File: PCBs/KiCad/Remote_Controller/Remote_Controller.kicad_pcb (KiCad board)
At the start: 2 copper layers, 83 parts, among them J201 USB_C_Receptacle_USB2.0_16P, Q101 IRF7309IPBF, Q102 IRFML8244TRPBF, Q103 IRFML8244TRPBF, Q201 SS8050-G, Q202 SS8050-G, SW101 Power Switch, SW201 SW_Push, SW301 SW_Push, SW302 SW_Push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

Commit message: Add board rules and stack up
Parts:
- Q101: value IRF7309IPBF -> IRF7319
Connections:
- net Net-(Q101A-G) renamed /[1] Power/PW_SW_R
- net Net-(Q101A-S) renamed /[1] Power/PW_SW_R_G_S
- net Net-(SW101-A) renamed /[1] Power/PWR_SW_CAP
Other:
- copper layers 2 -> 4

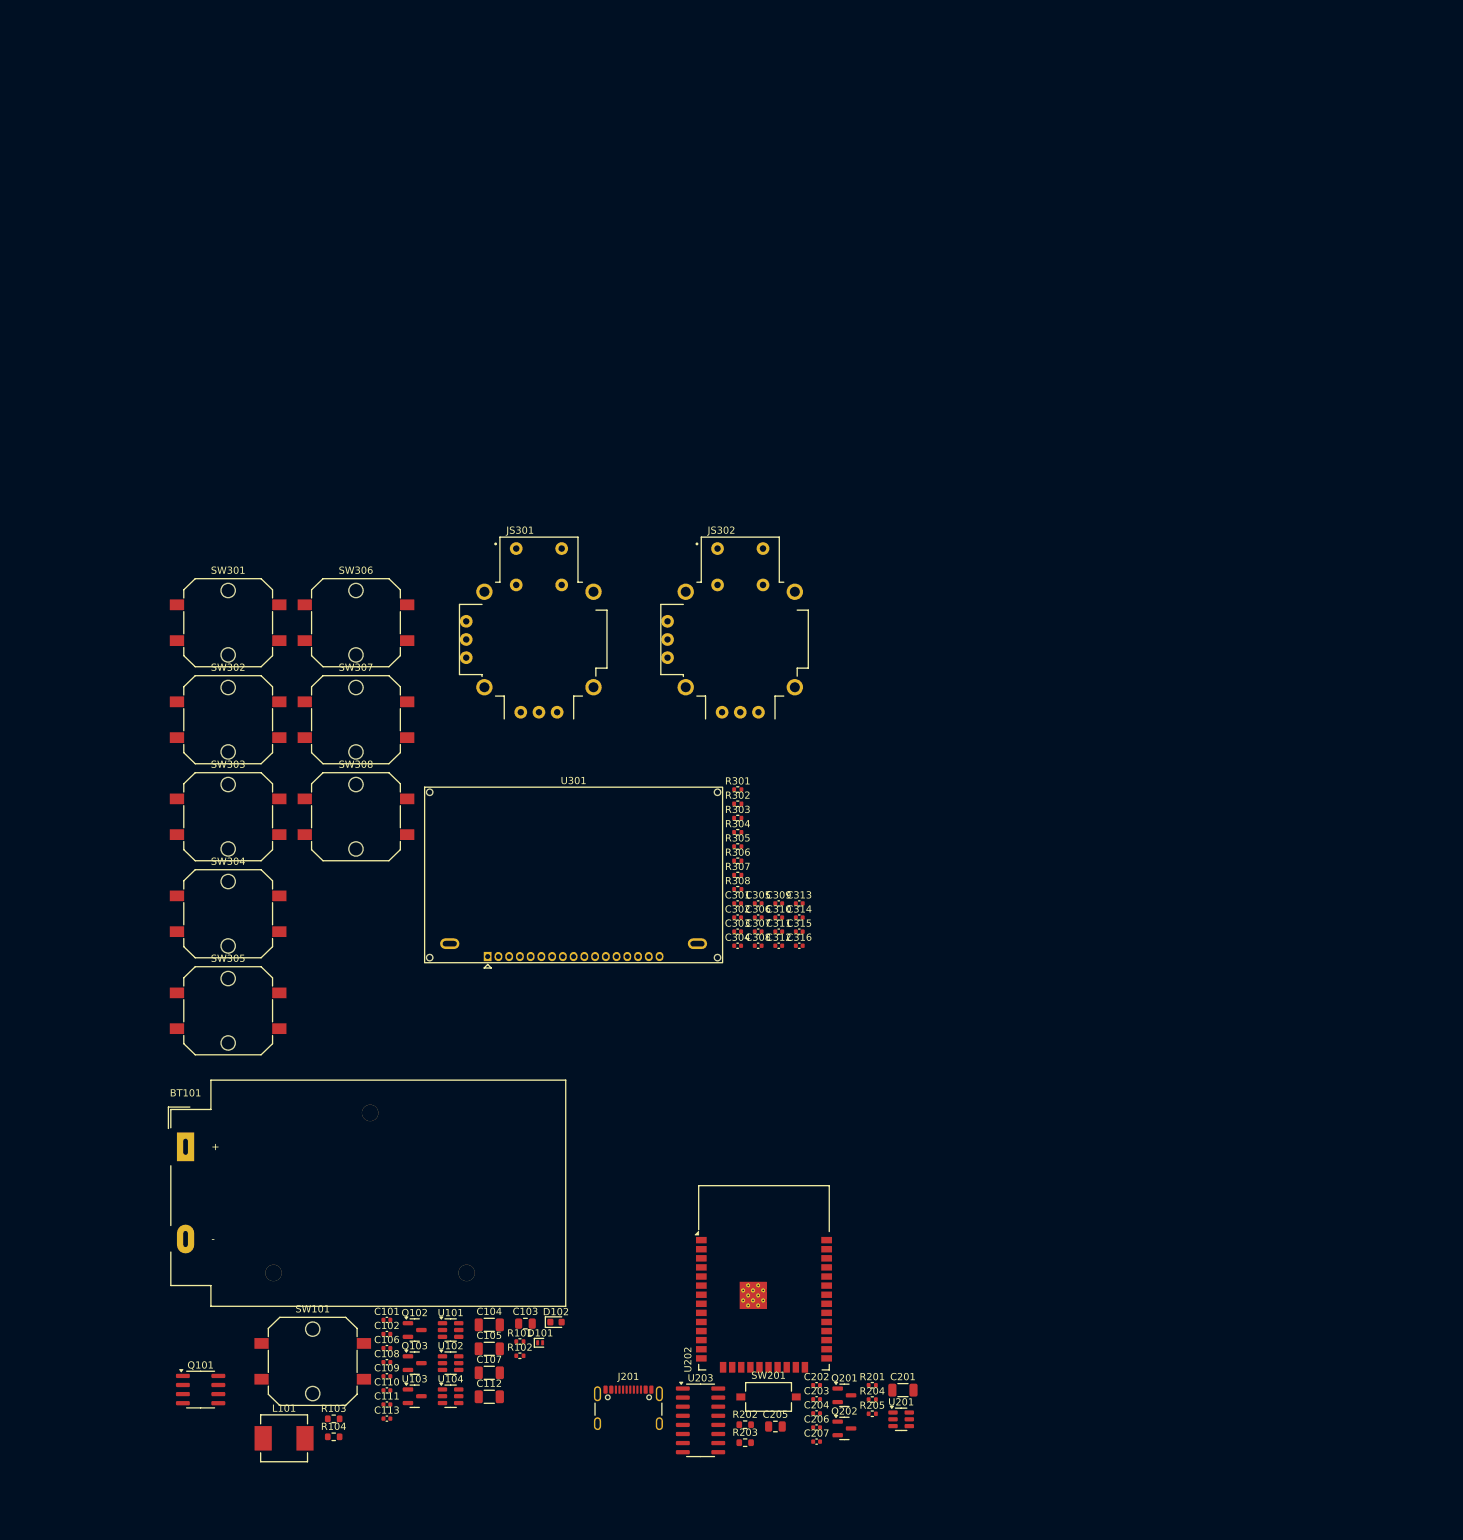
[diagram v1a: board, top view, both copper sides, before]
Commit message: Finish rough layout, add 3D model of ESP32, pushbuttons,  Display, tactile switch
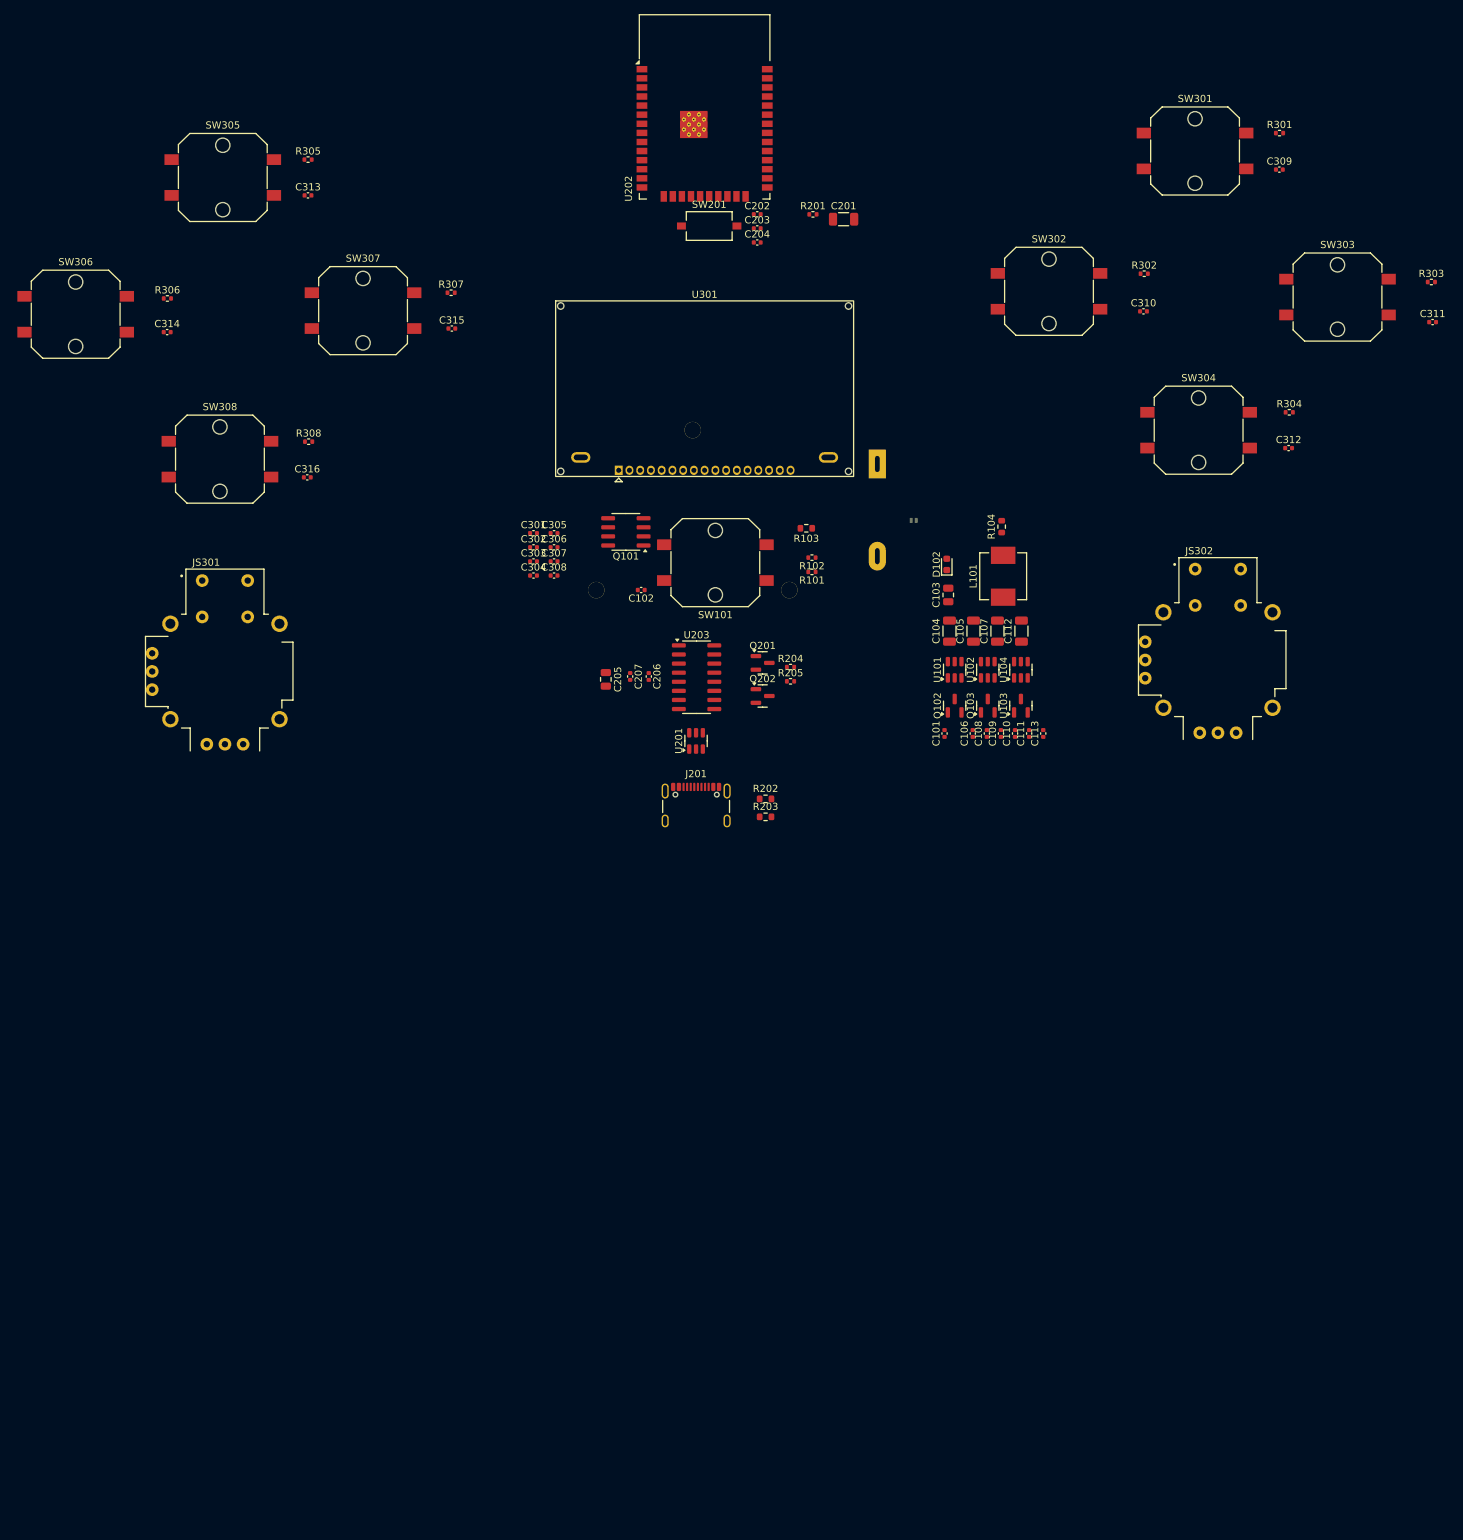
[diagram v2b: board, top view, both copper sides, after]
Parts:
- BT101, D101: moved to B.Cu
- moved SW303 171.1 mm to (228.9, -17.3)
- moved C201 163.8 mm to (159.9, -28.2)
- moved C202 163.8 mm to (147.8, -28.9)
- moved C203 163.8 mm to (147.8, -26.9)
- moved C204 163.8 mm to (147.8, -24.9)
- moved SW201 163.8 mm to (141.1, -27.2)
- moved U202 163.8 mm to (140.5, -40.9)
- moved R201 163.8 mm to (155.6, -28.9)
- moved R104 157.7 mm to (182.0, 14.8), turned to 90 degrees
- moved L101 156.8 mm to (182.2, 21.7), turned to 90 degrees
- moved SW304 151.4 mm to (209.5, 1.30)
- moved SW301 150.3 mm to (209.0, -37.7)
- moved R103 140.8 mm to (154.7, 15.0), turned to 180 degrees
- moved BT101 135.8 mm to (164.6, 6.01), turned to 180 degrees
- moved Q101 133.7 mm to (129.5, 15.5), turned to 180 degrees
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
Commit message: Reduced size of capacitor C201 to 0603 and corrected CH340 cap decoupler circuit, also improved PCB layout
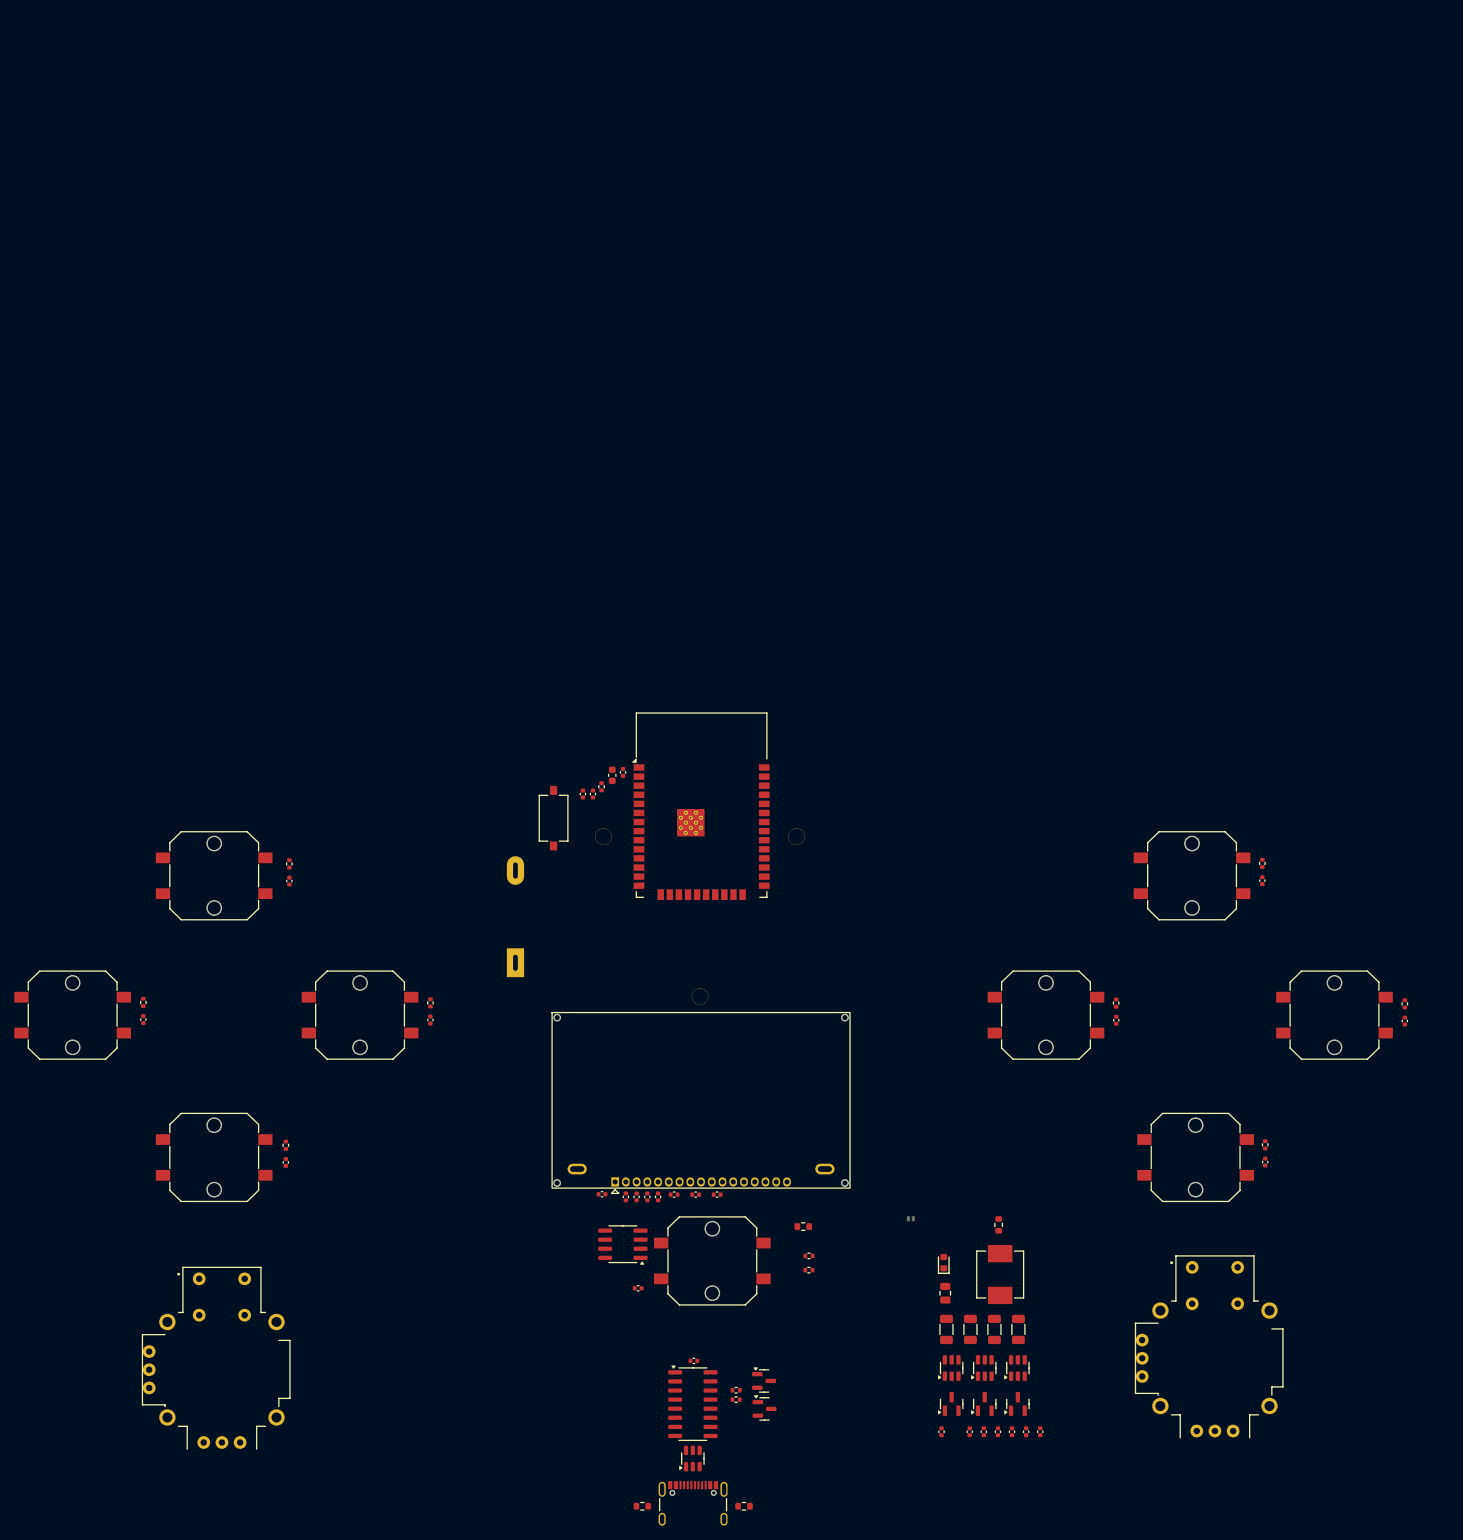
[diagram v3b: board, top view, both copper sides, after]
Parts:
- removed C205: 10uF, Capacitor_SMD:C_0805_2012Metric
- removed C207: 0.1uF, Capacitor_SMD:C_0402_1005Metric
- C201: footprint Capacitor_SMD:C_1206_3216Metric -> Capacitor_SMD:C_0603_1608Metric
- moved Q201 104.2 mm to (148.9, 138.0)
- moved R304 102.4 mm to (218.8, 101.1), turned to 90 degrees
- moved R301 102.0 mm to (218.4, 61.8), turned to 90 degrees
- moved R302 102.0 mm to (198.0, 81.3), turned to 90 degrees
- moved SW304 101.6 mm to (209.1, 102.9)
- moved U203 101.5 mm to (138.9, 137.3)
- moved R204 101.3 mm to (144.9, 135.4)
- moved SW301 101.2 mm to (208.6, 63.5)
- moved SW302 101.1 mm to (188.2, 83.0)
- moved R303 100.9 mm to (238.3, 81.4), turned to 90 degrees
- moved R205 100.6 mm to (144.9, 136.7)
- moved SW303 100.3 mm to (228.5, 83.0)
- moved R202 100.3 mm to (131.8, 151.6), turned to 180 degrees
- moved U201 100.2 mm to (138.9, 144.9)
- moved C312 99.8 mm to (218.8, 103.5), turned to -90 degrees
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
